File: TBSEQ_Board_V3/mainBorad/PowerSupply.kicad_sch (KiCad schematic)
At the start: 23 parts, among them IC4 NJM2125F-TE1

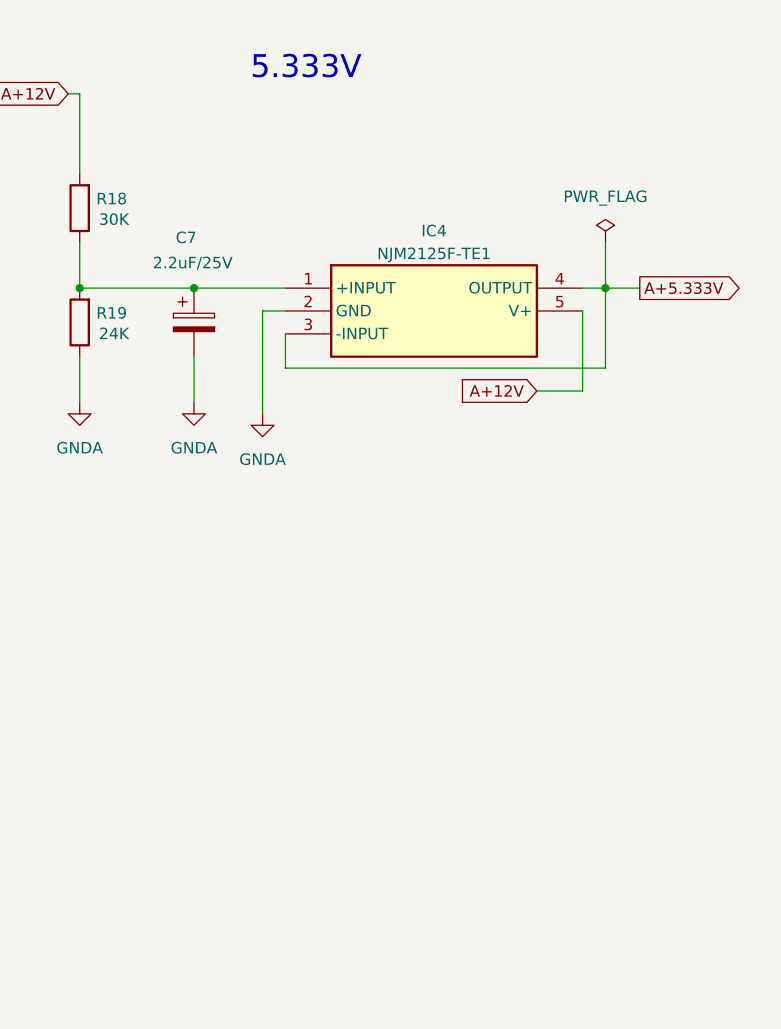
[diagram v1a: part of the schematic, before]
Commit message: V3Board
DualTr OPAmp やはりDIPに変更してオートルーター前に戻す
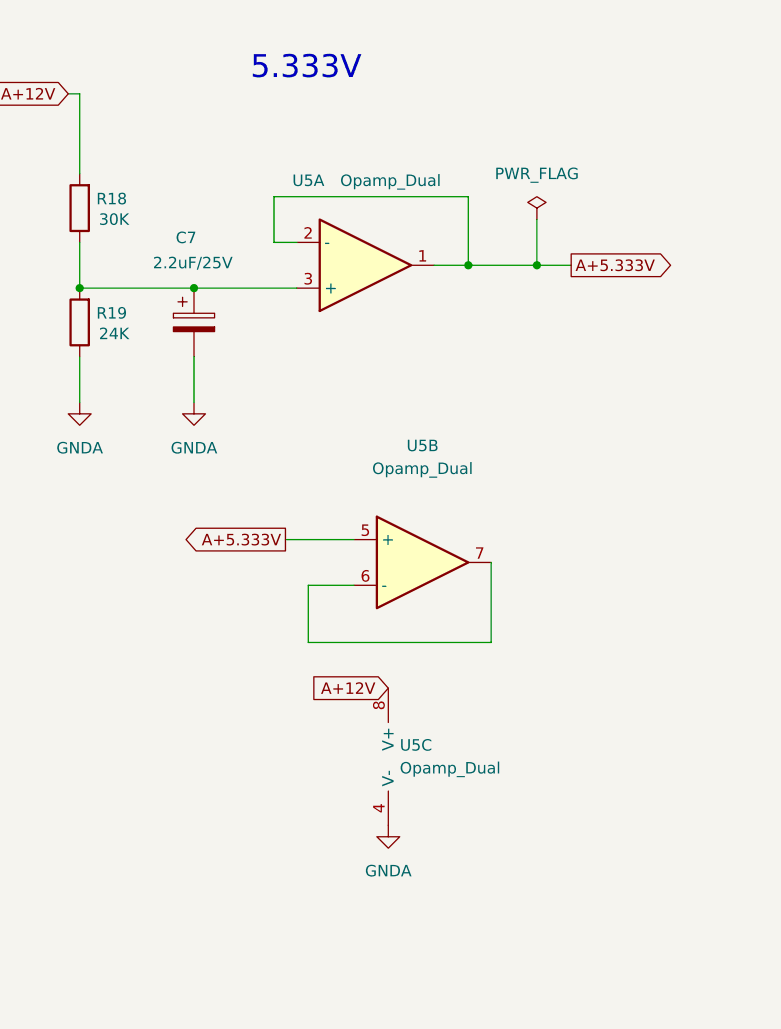
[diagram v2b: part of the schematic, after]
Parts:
- removed IC4: NJM2125F-TE1, SOT95P280X130-5N, symbol SamacSys_Parts:NJM2125F-TE1
- added U5: Opamp_Dual, Package_DIP:DIP-8_W7.62mm_LongPads, symbol Device:Opamp_Dual
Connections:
- net A+12V: now also U5.8 (V+)
- net A+5.333V: now also U5.1, U5.2 (-), U5.5 (+)
- net GNDA: now also U5.4 (V-)
- net at C7.1, R18.1, R19.2: now also U5.3 (+)
- new net: U5.6 (-), U5.7

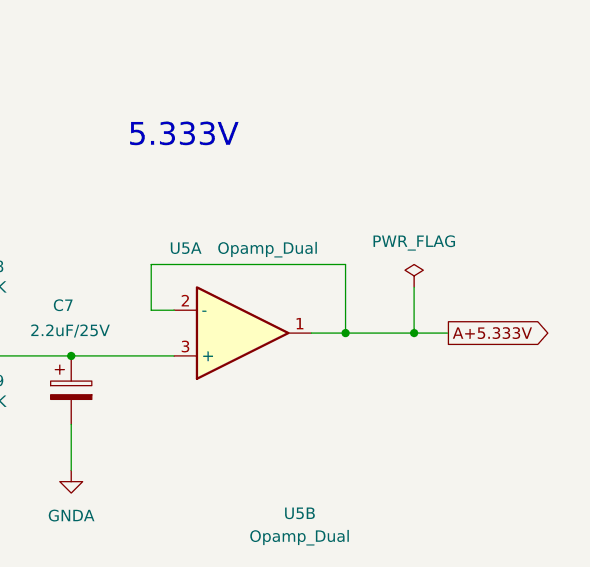
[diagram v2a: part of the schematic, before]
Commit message: V3Board
ERCチェック修正中
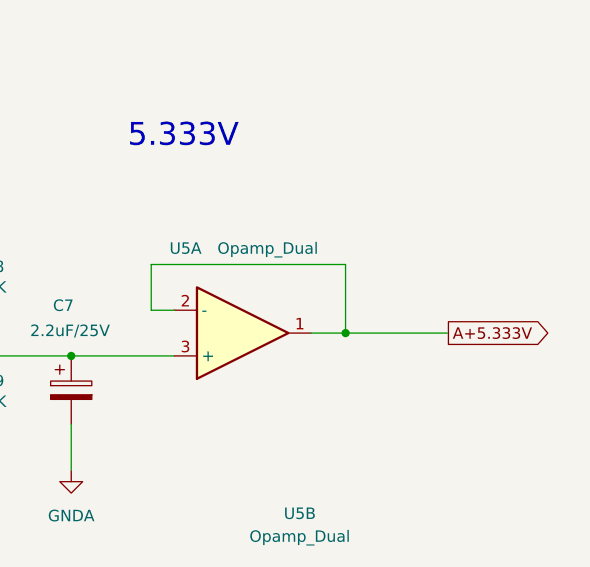
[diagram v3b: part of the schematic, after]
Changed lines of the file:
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@@
 	)
 	(junction
-		(at 259.08 64.77)
-		(diameter 0)
-		(color 0 0 0 0)
-	)
-	(junction
 		(at 144.78 133.35)
 		(diameter 0)
@@
 	(wire
 		(pts
-			(xy 259.08 64.77) (xy 262.89 64.77)
+			(xy 251.46 64.77) (xy 262.89 64.77)
 		)
 		(stroke
@@
 	(wire
 		(pts
-			(xy 251.46 64.77) (xy 259.08 64.77)
-		)
-		(stroke
-			(width 0)
-			(type default)
-		)
-	)
-	(wire
-		(pts
-			(xy 259.08 59.69) (xy 259.08 64.77)
-		)
-		(stroke
-			(width 0)
-			(type default)
-		)
-	)
-	(wire
-		(pts
 			(xy 137.16 45.72) (xy 146.05 45.72)
 		)
@@
 					(unit 1)
 				)
-			)
-		)
-	)
-	(symbol
-		(lib_id "power:PWR_FLAG")
-		(at 259.08 59.69 0)
-		(unit 1)
-		(exclude_from_sim no)
-		(in_bom yes)
-		(on_board yes)
-		(dnp no)
-		(fields_autoplaced yes)
-		(property "Reference" "#FLG011"
-			(at 259.08 57.785 0)
-			(effects
-				(font
-					(size 1.27 1.27)
-				)
-				(hide yes)
-			)
-		)
-		(property "Value" "PWR_FLAG"
-			(at 259.08 54.61 0)
-			(effects
-				(font
-					(size 1.27 1.27)
-				)
-			)
-		)
-		(property "Footprint" ""
-			(at 259.08 59.69 0)
-			(effects
-				(font
-					(size 1.27 1.27)
-				)
-				(hide yes)
-			)
-		)
-		(property "Datasheet" "~"
-			(at 259.08 59.69 0)
-			(effects
-				(font
-					(size 1.27 1.27)
-				)
-				(hide yes)
-			)
-		)
-		(property "Description" "Special symbol for telling ERC where power comes from"
-			(at 259.08 59.69 0)
-			(effects
-				(font
-					(size 1.27 1.27)
-				)
-				(hide yes)
-			)
-		)
-		(pin "1"
-		)
-		(instances
-			(project "mainBorad"
-				(path "/83af791a-9776-40a7-82ad-9528ff7474b8/7067d32e-232c-4c33-be2e-744ed9661c4e"
-					(reference "#FLG011")
-					(unit 1)
-				)
